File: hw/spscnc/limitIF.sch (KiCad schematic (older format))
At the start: 22 parts, among them J20 8P8C_4xShielded, J5 Limit_IF

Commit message: .
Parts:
- removed R64, R65: 10K, Resistor_SMD:R_0805_2012Metric, symbol Device:R
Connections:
- net +3V3: no longer J5.8 (Pin_8)
- net RESET_BTN: now reaches J20.3, R140.1
- net RESET_BTN: now also J5.8 (Pin_8)
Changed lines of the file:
@@
-$EndComp
-$Comp
-L Device:R R?
-U 1 1 61E9D2BC
-P 2875 5575
-AR Path="/61C80DFB/61E9D2BC" Ref="R?"  Part="1"
-AR Path="/61CA9588/61E9D2BC" Ref="R?"  Part="1"
-AR Path="/61E6D951/61E9D2BC" Ref="R64"  Part="1"
-F 0 "R64" V 2875 5550 50  0000 C CNN
-F 1 "10K" V 2759 5575 50  0000 C CNN
-F 2 "Resistor_SMD:R_0805_2012Metric" V 2805 5575 50  0001 C CNN
-F 3 "~" H 2875 5575 50  0001 C CNN
-F 4 "C17414" H 2875 5575 50  0001 C CNN "jlcpcb"
-	1    2875 5575
-	-1   0    0    1
-$EndComp
-$Comp
-L industrial:+3V3 #PWR?
-U 1 1 61E9D2C2
-P 2875 5425
-AR Path="/61C80DFB/61E9D2C2" Ref="#PWR?"  Part="1"
-AR Path="/61CA9588/61E9D2C2" Ref="#PWR?"  Part="1"
-AR Path="/61E6D951/61E9D2C2" Ref="#PWR016"  Part="1"
-F 0 "#PWR016" H 2875 5275 50  0001 C CNN
-F 1 "+3V3" H 2890 5598 50  0000 C CNN
-F 2 "" H 2875 5425 50  0001 C CNN
-F 3 "" H 2875 5425 50  0001 C CNN
-	1    2875 5425
-	1    0    0    -1
 $EndComp
 $Comp
@@
 	1    2675 5425
 	1    0    0    -1
-$EndComp
-$Comp
-L Device:R R?
-U 1 1 61E9D2CF
-P 3075 5575
-AR Path="/61C80DFB/61E9D2CF" Ref="R?"  Part="1"
-AR Path="/61CA9588/61E9D2CF" Ref="R?"  Part="1"
-AR Path="/61E6D951/61E9D2CF" Ref="R65"  Part="1"
-F 0 "R65" V 3075 5550 50  0000 C CNN
-F 1 "10K" V 2959 5575 50  0000 C CNN
-F 2 "Resistor_SMD:R_0805_2012Metric" V 3005 5575 50  0001 C CNN
-F 3 "~" H 3075 5575 50  0001 C CNN
-F 4 "C17414" H 3075 5575 50  0001 C CNN "jlcpcb"
-	1    3075 5575
-	-1   0    0    1
 $EndComp
 $Comp
@@
 $Comp
 L industrial:+3V3 #PWR?
-U 1 1 61E9D2DC
-P 3075 5425
-AR Path="/61C80DFB/61E9D2DC" Ref="#PWR?"  Part="1"
-AR Path="/61CA9588/61E9D2DC" Ref="#PWR?"  Part="1"
-AR Path="/61E6D951/61E9D2DC" Ref="#PWR0129"  Part="1"
-F 0 "#PWR0129" H 3075 5275 50  0001 C CNN
-F 1 "+3V3" H 3090 5598 50  0000 C CNN
-F 2 "" H 3075 5425 50  0001 C CNN
-F 3 "" H 3075 5425 50  0001 C CNN
-	1    3075 5425
-	1    0    0    -1
-$EndComp
-$Comp
-L industrial:+3V3 #PWR?
 U 1 1 61E9D2E2
 P 3300 5425
@@
 Wire Wire Line
 	3425 6350 3300 6350
-Wire Wire Line
-	3075 5725 3075 5950
 Connection ~ 3075 5950
 Wire Wire Line
@@
 Wire Wire Line
 	4100 6150 2875 6150
-Connection ~ 2875 6150
-Wire Wire Line
-	2875 5725 2875 6150
 $Comp
 L Device:C C?
@@
 $Comp
 L industrial:+3V3 #PWR?
-U 1 1 61EB2C87
-P 3325 4275
-AR Path="/61CA9588/61EB2C87" Ref="#PWR?"  Part="1"
-AR Path="/61E6D951/61EB2C87" Ref="#PWR0133"  Part="1"
-F 0 "#PWR0133" H 3325 4125 50  0001 C CNN
-F 1 "+3V3" V 3325 4525 50  0000 C CNN
-F 2 "" H 3325 4275 50  0001 C CNN
-F 3 "" H 3325 4275 50  0001 C CNN
-	1    3325 4275
-	0    -1   -1   0
-$EndComp
-$Comp
-L industrial:+3V3 #PWR?
 U 1 1 61EB35CC
 P 3825 4275
@@
 	0    1    1    0
 $EndComp
+Text Label 3950 5950 0    50   ~ 0
+RESET_BTN
+Text Label 3325 4275 2    50   ~ 0
+RESET_BTN
 $EndSCHEMATC

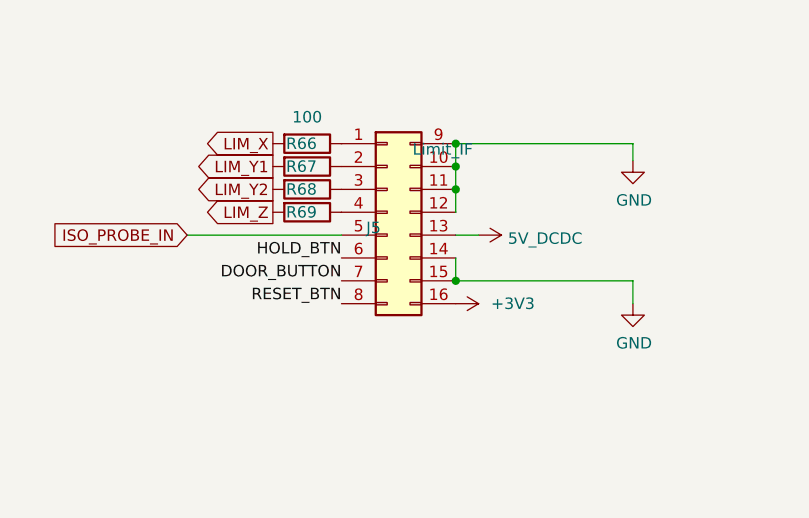
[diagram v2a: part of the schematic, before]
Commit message: added most corrections on the schematic for i2s operation.
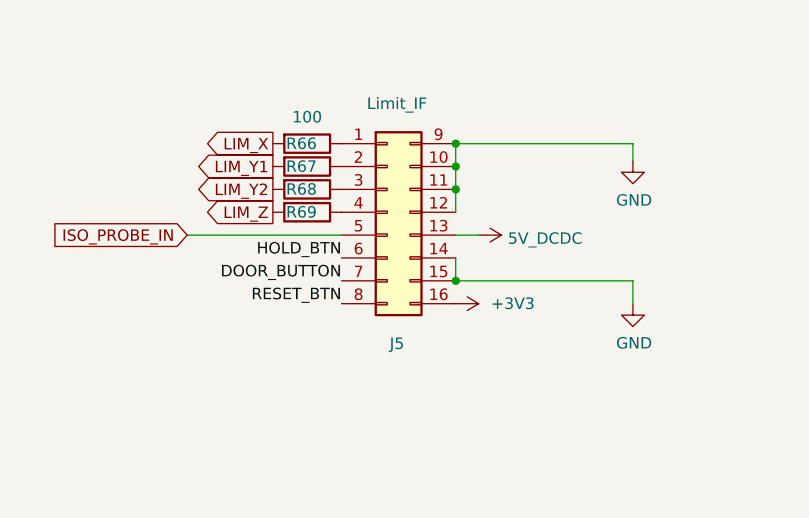
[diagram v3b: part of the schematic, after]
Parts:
- J20: footprint industrial000:rj45_R-RJ45S08P-B000_C386763 -> industrial:rj45_R-RJ45S08P-B000_C386763
- J5: footprint industrial000:connRPC2x8_3.5mm2.5mm -> industrial:connRPC2x8_3.5mm2.5mm
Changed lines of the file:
@@
 $Descr A4 11693 8268
 encoding utf-8
-Sheet 13 16
+Sheet 13 17
 Title "Trinamic FluidNC CNC Controller"
 Date "2022-01-27"
@@
 AR Path="/61CEF4C9/61E712B0" Ref="J?"  Part="1"
 AR Path="/61E6D951/61E712B0" Ref="J5"  Part="1"
-F 0 "J5" H 3497 3807 50  0000 R CNN
-F 1 "Limit_IF" H 3900 4150 50  0000 R CNN
-F 2 "industrial000:connRPC2x8_3.5mm2.5mm" H 3525 3875 50  0001 C CNN
+F 0 "J5" H 3600 3300 50  0000 R CNN
+F 1 "Limit_IF" H 3700 4350 50  0000 R CNN
+F 2 "industrial:connRPC2x8_3.5mm2.5mm" H 3525 3875 50  0001 C CNN
 F 3 "~" H 3525 3875 50  0001 C CNN
 F 4 "DNP020" H 3525 3875 50  0001 C CNN "jlcpcb"
@@
 F 0 "J20" H 4720 5972 50  0000 R CNN
 F 1 "8P8C_4xShielded" H 4720 6063 50  0000 R CNN
-F 2 "industrial000:rj45_R-RJ45S08P-B000_C386763" V 5050 6075 50  0001 C CNN
+F 2 "industrial:rj45_R-RJ45S08P-B000_C386763" V 5050 6075 50  0001 C CNN
 F 3 "~" V 5050 6075 50  0001 C CNN
 F 4 "DNP007" H 5050 6050 50  0001 C CNN "jlcpcb"

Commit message: Finished preliminary routing, pending checklist and review
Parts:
- added R192, R65: 10K, Resistor_SMD:R_0805_2012Metric, symbol Device:R
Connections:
- net +3V3: now also R192.2, R65.2
- net GND: no longer J5.11 (Pin_11), J5.12 (Pin_12)
- new net LIM_A: J5.12 (Pin_12), R65.1
- new net LIM_B: J5.11 (Pin_11), R192.1
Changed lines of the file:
@@
 $EndComp
-Wire Wire Line
-	3825 3775 3825 3675
 Wire Wire Line
 	3825 3675 3825 3575
-Connection ~ 3825 3675
 Wire Wire Line
 	3825 3575 4600 3575
@@
 Wire Wire Line
 	3925 3975 3825 3975
-Wire Wire Line
-	3825 3875 3825 3775
-Connection ~ 3825 3775
 $Comp
 L industrial:8P8C_4xShielded J?
@@
 Text Label 3325 4275 2    50   ~ 0
 RESET_BTN
+Text GLabel 8450 5175 3    50   Output ~ 0
+LIM_B
+Text GLabel 8200 5175 3    50   Output ~ 0
+LIM_A
+$Comp
+L Device:R R?
+U 1 1 62172151
+P 8200 5025
+AR Path="/61C80DFB/62172151" Ref="R?"  Part="1"
+AR Path="/61C80E48/62172151" Ref="R?"  Part="1"
+AR Path="/61C80E8F/62172151" Ref="R?"  Part="1"
+AR Path="/61CEF4C9/62172151" Ref="R?"  Part="1"
+AR Path="/61E6D951/62172151" Ref="R65"  Part="1"
+F 0 "R65" V 8200 5000 50  0000 C CNN
+F 1 "10K" V 8084 5025 50  0000 C CNN
+F 2 "Resistor_SMD:R_0805_2012Metric" V 8130 5025 50  0001 C CNN
+F 3 "~" H 8200 5025 50  0001 C CNN
+F 4 "C17414" H 8200 5025 50  0001 C CNN "jlcpcb"
+	1    8200 5025
+	-1   0    0    1
+$EndComp
+$Comp
+L industrial:+3V3 #PWR?
+U 1 1 6217215B
+P 8200 4875
+AR Path="/61C80DFB/6217215B" Ref="#PWR?"  Part="1"
+AR Path="/61C80E48/6217215B" Ref="#PWR?"  Part="1"
+AR Path="/61C80E8F/6217215B" Ref="#PWR?"  Part="1"
+AR Path="/61CEF4C9/6217215B" Ref="#PWR?"  Part="1"
+AR Path="/61E6D951/6217215B" Ref="#PWR0169"  Part="1"
+F 0 "#PWR0169" H 8200 4725 50  0001 C CNN
+F 1 "+3V3" H 8215 5048 50  0000 C CNN
+F 2 "" H 8200 4875 50  0001 C CNN
+F 3 "" H 8200 4875 50  0001 C CNN
+	1    8200 4875
+	1    0    0    -1
+$EndComp
+$Comp
+L Device:R R?
+U 1 1 62172166
+P 8450 5025
+AR Path="/61C80DFB/62172166" Ref="R?"  Part="1"
+AR Path="/61C80E48/62172166" Ref="R?"  Part="1"
+AR Path="/61C80E8F/62172166" Ref="R?"  Part="1"
+AR Path="/61CEF4C9/62172166" Ref="R?"  Part="1"
+AR Path="/61E6D951/62172166" Ref="R192"  Part="1"
+F 0 "R192" V 8450 5000 50  0000 C CNN
+F 1 "10K" V 8334 5025 50  0000 C CNN
+F 2 "Resistor_SMD:R_0805_2012Metric" V 8380 5025 50  0001 C CNN
+F 3 "~" H 8450 5025 50  0001 C CNN
+F 4 "C17414" H 8450 5025 50  0001 C CNN "jlcpcb"
+	1    8450 5025
+	-1   0    0    1
+$EndComp
+$Comp
+L industrial:+3V3 #PWR?
+U 1 1 62172170
+P 8450 4875
+AR Path="/61C80DFB/62172170" Ref="#PWR?"  Part="1"
+AR Path="/61C80E48/62172170" Ref="#PWR?"  Part="1"
+AR Path="/61C80E8F/62172170" Ref="#PWR?"  Part="1"
+AR Path="/61CEF4C9/62172170" Ref="#PWR?"  Part="1"
+AR Path="/61E6D951/62172170" Ref="#PWR0170"  Part="1"
+F 0 "#PWR0170" H 8450 4725 50  0001 C CNN
+F 1 "+3V3" H 8465 5048 50  0000 C CNN
+F 2 "" H 8450 4875 50  0001 C CNN
+F 3 "" H 8450 4875 50  0001 C CNN
+	1    8450 4875
+	1    0    0    -1
+$EndComp
+Text GLabel 3900 3775 2    50   Output ~ 0
+LIM_B
+Text GLabel 3900 3875 2    50   Output ~ 0
+LIM_A
+Wire Wire Line
+	3900 3775 3825 3775
+Wire Wire Line
+	3825 3875 3900 3875
 $EndSCHEMATC

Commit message: As ordered 1.0.1
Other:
- note added: "The system is designed for NC switches.\nThis allows detecting if the sensor is not in place\nIn particular, LIM_A not being connected may affect the flash\nbehavior (MTDO)"
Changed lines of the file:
@@
 Sheet 13 17
 Title "Trinamic FluidNC CNC Controller"
-Date "2022-01-27"
-Rev "1.0.0"
+Date "2022-02-12"
+Rev "1.0.1"
 Comp ""
 Comment1 "Limit sensor connectors"
@@
 Wire Wire Line
 	3825 3875 3900 3875
+Text Notes 4100 2500 0    50   ~ 0
+The system is designed for NC switches.\nThis allows detecting if the sensor is not in place\nIn particular, LIM_A not being connected may affect the flash\nbehavior (MTDO)
 $EndSCHEMATC
